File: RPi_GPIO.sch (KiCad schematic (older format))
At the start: 19 parts, among them J1 CONN_02X19, J2 RPi_GPIO, J3 CONN_02X06, J4 CONN_02X06, J5 CONN_02X06, J6 CONN_02X10, J7 CONN_02X10, J8 CONN_02X10, U1 DS1307Z+, U2 CAT24C32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

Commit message: cleanup and add RX/TX header
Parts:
- removed C1: CAP, Capacitors_SMD:C_0805_HandSoldering, symbol CAP
- removed R1: R, Resistors_SMD:R_0805_HandSoldering, symbol R
- added J9: CONN_01X04, Pin_Headers:Pin_Header_Straight_1x04_Pitch2.54mm, symbol CONN_01X04
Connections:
- net 3.3V: now also J3.1 (P1), J8.1 (P1), J9.1 (P1)
- net GND: now also J5.2 (P2), J6.2 (P2), J9.2 (P2)
- net Pin10 renamed RX
- net RX: now also J9.4 (P4)
- net Pin8 renamed TX
- net TX: now also J9.3 (P3)
- no-connect marks 0 -> 1
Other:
- note removed: "100nf"
- note removed: "10K"
- moved on the sheet: J7, J8
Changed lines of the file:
@@
 EESchema Schematic File Version 2
-LIBS:RPi_Hat-rescue
 LIBS:power
 LIBS:device
@@
 LIBS:Zilog
 LIBS:cat24c32
-LIBS:ds1340
 LIBS:RPi_Hat-cache
 EELAYER 25 0
@@
 GND
 Text GLabel 9200 3000 2    60   Input ~ 0
-Pin8
+TX
 Text GLabel 9200 3100 2    60   Input ~ 0
-Pin10
+RX
 Text GLabel 9200 3200 2    60   Input ~ 0
 Pin12
@@
 GND
 Text GLabel 5750 3100 2    60   Input ~ 0
-Pin8
+TX
 Text GLabel 5750 3200 2    60   Input ~ 0
-Pin10
+RX
 Text GLabel 5750 3300 2    60   Input ~ 0
 Pin12
@@
 Text GLabel 4350 7100 3    60   Input ~ 0
 GND
-$Comp
-L R R1
-U 1 1 598AB3BE
-P 5200 6200
-F 0 "R1" V 5280 6200 50  0000 C CNN
-F 1 "R" V 5200 6200 50  0000 C CNN
-F 2 "Resistors_SMD:R_0805_HandSoldering" V 5130 6200 50  0001 C CNN
-F 3 "" H 5200 6200 50  0001 C CNN
-	1    5200 6200
-	0    -1   -1   0
-$EndComp
-$Comp
-L CAP C1
-U 1 1 598AB3EF
-P 5800 6200
-F 0 "C1" V 5900 6350 50  0000 C CNN
-F 1 "CAP" V 5900 6050 50  0000 C CNN
-F 2 "Capacitors_SMD:C_0805_HandSoldering" H 5800 6200 50  0001 C CNN
-F 3 "" H 5800 6200 50  0001 C CNN
-	1    5800 6200
-	0    -1   -1   0
-$EndComp
-Text GLabel 6050 6200 2    60   Input ~ 0
-GND
-Text Notes 5900 6450 2    60   ~ 0
-100nf
-Text Notes 5300 6350 2    60   ~ 0
-10K
 Text Notes 3050 5950 2    60   ~ 0
 32.768Hz
@@
 	4350 7500 4950 7500
 Wire Wire Line
-	4950 6200 5050 6200
-Wire Wire Line
-	5350 6200 5550 6200
-Wire Wire Line
 	3000 2150 2650 2150
 Wire Wire Line
@@
 L CONN_02X10 J7
 U 1 1 598D0311
-P 2600 5150
-F 0 "J7" H 2600 5700 50  0000 C CNN
-F 1 "CONN_02X10" V 2600 5150 50  0000 C CNN
-F 2 "Pin_Headers:Pin_Header_Straight_2x10_Pitch2.54mm" H 2600 3950 50  0001 C CNN
-F 3 "" H 2600 3950 50  0001 C CNN
-	1    2600 5150
+P 2800 5150
+F 0 "J7" H 2800 5700 50  0000 C CNN
+F 1 "CONN_02X10" V 2800 5150 50  0000 C CNN
+F 2 "Pin_Headers:Pin_Header_Straight_2x10_Pitch2.54mm" H 2800 3950 50  0001 C CNN
+F 3 "" H 2800 3950 50  0001 C CNN
+	1    2800 5150
 	1    0    0    -1
 $EndComp
@@
 L CONN_02X10 J8
 U 1 1 598D0360
-P 3200 5150
-F 0 "J8" H 3200 5700 50  0000 C CNN
-F 1 "CONN_02X10" V 3200 5150 50  0000 C CNN
-F 2 "Pin_Headers:Pin_Header_Straight_2x10_Pitch2.54mm" H 3200 3950 50  0001 C CNN
-F 3 "" H 3200 3950 50  0001 C CNN
-	1    3200 5150
-	1    0    0    -1
-$EndComp
+P 3650 5200
+F 0 "J8" H 3650 5750 50  0000 C CNN
+F 1 "CONN_02X10" V 3650 5200 50  0000 C CNN
+F 2 "Pin_Headers:Pin_Header_Straight_2x10_Pitch2.54mm" H 3650 4000 50  0001 C CNN
+F 3 "" H 3650 4000 50  0001 C CNN
+	1    3650 5200
+	1    0    0    -1
+$EndComp
+NoConn ~ 4950 6200
+$Comp
+L CONN_01X04 J9
+U 1 1 59918E85
+P 8700 5800
+F 0 "J9" H 8700 6050 50  0000 C CNN
+F 1 "CONN_01X04" V 8800 5800 50  0000 C CNN
+F 2 "Pin_Headers:Pin_Header_Straight_1x04_Pitch2.54mm" H 8700 5800 50  0001 C CNN
+F 3 "" H 8700 5800 50  0001 C CNN
+	1    8700 5800
+	1    0    0    -1
+$EndComp
+Text GLabel 8500 5650 0    60   Input ~ 0
+3.3V
+Text GLabel 8500 5750 0    60   Input ~ 0
+GND
+Text GLabel 8500 5850 0    60   Input ~ 0
+TX
+Text GLabel 8500 5950 0    60   Input ~ 0
+RX
+Text GLabel 3400 4750 0    60   Input ~ 0
+3.3V
+Text GLabel 2250 4700 2    60   Input ~ 0
+GND
+Text GLabel 1750 3850 0    60   Input ~ 0
+3.3V
+Text GLabel 3450 3850 2    60   Input ~ 0
+GND
 $EndSCHEMATC

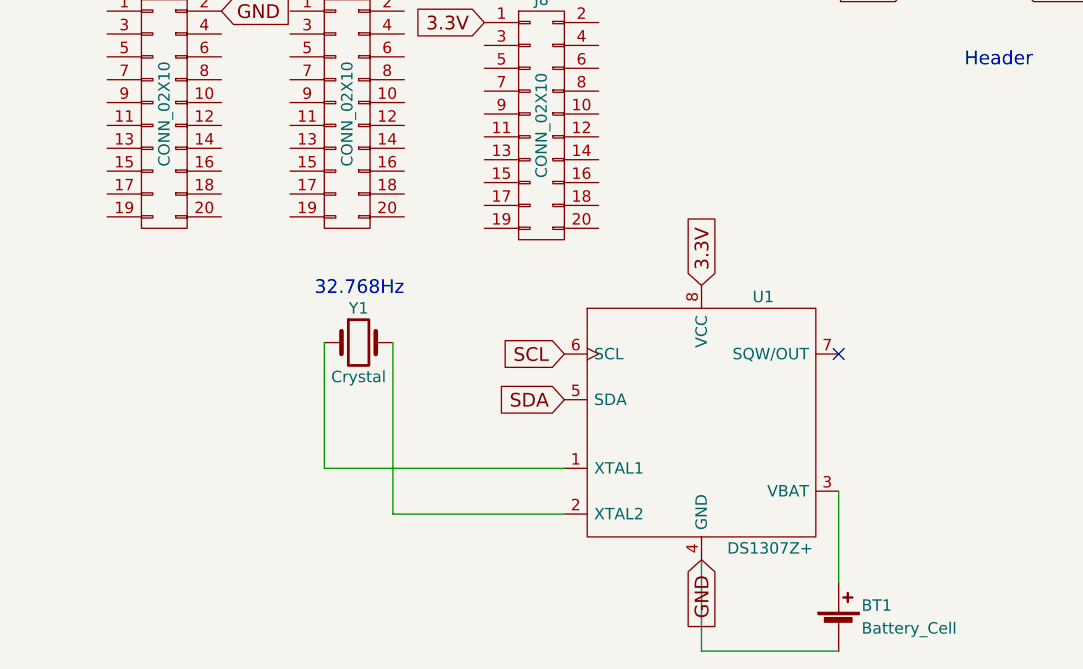
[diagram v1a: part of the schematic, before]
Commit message: support MCP7940N as well as ds1338/ds1340
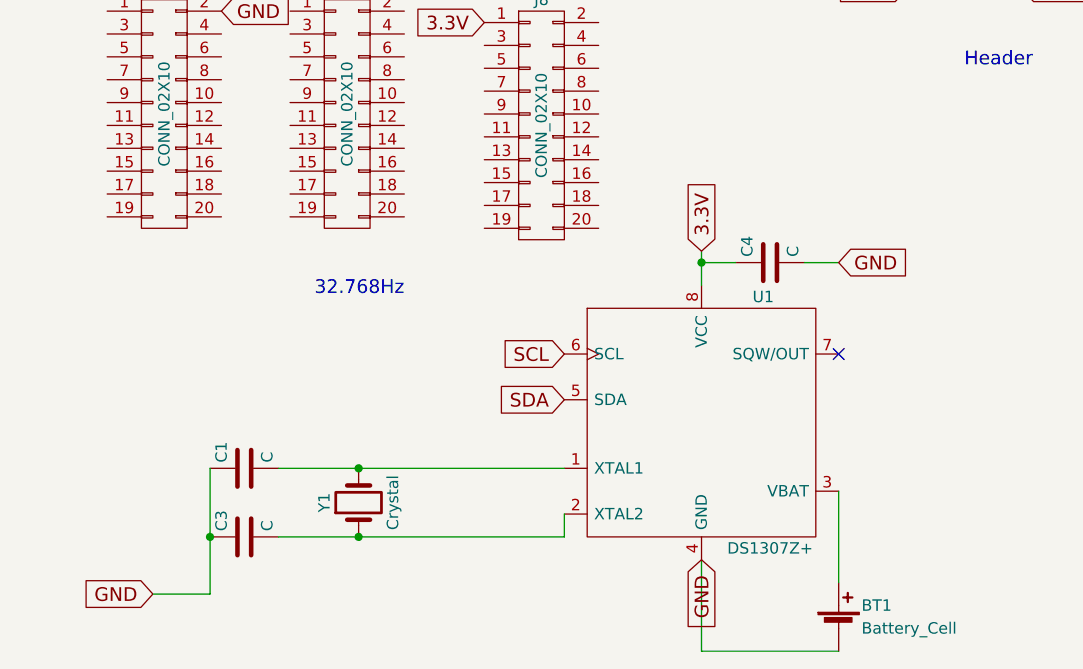
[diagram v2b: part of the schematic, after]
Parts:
- added C1, C3, C4: C, Capacitors_SMD:C_0805_HandSoldering, symbol C
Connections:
- net 3.3V: now also C4.1
- net GND: now also C1.1, C3.1, C4.2
- net at Y1.1: now also U1.2 (XTAL2), C3.2; no longer U1.1 (XTAL1)
- net at Y1.2: now also U1.1 (XTAL1), C1.2; no longer U1.2 (XTAL2)
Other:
- moved on the sheet: Y1
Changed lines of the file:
@@
 L Crystal Y1
 U 1 1 598A4A0E
-P 2850 6150
-F 0 "Y1" H 2850 6300 50  0000 C CNN
-F 1 "Crystal" H 2850 6000 50  0000 C CNN
-F 2 "Crystals:Crystal_SMD_EuroQuartz_EQ161-2pin_3.2x1.5mm_HandSoldering" H 2850 6150 50  0001 C CNN
-F 3 "" H 2850 6150 50  0001 C CNN
-	1    2850 6150
-	1    0    0    -1
+P 2850 6850
+F 0 "Y1" H 2850 7000 50  0000 C CNN
+F 1 "Crystal" H 2850 6700 50  0000 C CNN
+F 2 "Crystals:Crystal_SMD_EuroQuartz_EQ161-2pin_3.2x1.5mm_HandSoldering" H 2850 6850 50  0001 C CNN
+F 3 "" H 2850 6850 50  0001 C CNN
+	1    2850 6850
+	0    -1   -1   0
 $EndComp
 $Comp
@@
 	1    0    0    -1
 $EndComp
-Text GLabel 4350 5900 1    60   Input ~ 0
+Text GLabel 4350 5750 1    60   Input ~ 0
 3.3V
 Text GLabel 3750 6400 0    60   Input ~ 0
@@
 Text Notes 3700 2000 0    60   ~ 0
 3.9K
-Wire Wire Line
-	3750 6700 2700 6700
-Wire Wire Line
-	2700 6700 2700 6150
-Wire Wire Line
-	3750 6900 3000 6900
-Wire Wire Line
-	3000 6900 3000 6150
-Wire Wire Line
-	4950 6800 4950 7200
-Wire Wire Line
-	4350 7100 4350 7500
-Wire Wire Line
-	4350 7500 4950 7500
-Wire Wire Line
-	3000 2150 2650 2150
-Wire Wire Line
-	3000 1350 3000 2150
-Wire Wire Line
-	2700 1600 3000 1600
-Connection ~ 3000 1600
-Wire Wire Line
-	2650 2550 4050 2550
-Wire Wire Line
-	2650 2750 4050 2750
-Wire Wire Line
-	3250 1700 3250 1350
-Wire Wire Line
-	3600 1350 3600 1700
-Wire Wire Line
-	3950 1350 3950 1700
-Wire Wire Line
-	3950 2750 3950 2000
-Connection ~ 3950 2750
-Wire Wire Line
-	3600 2000 3600 2550
-Connection ~ 3600 2550
-Wire Wire Line
-	3250 2350 3250 2000
-Wire Wire Line
-	2650 2350 3250 2350
 $Comp
 L Jumper_NO_Small JP1
@@
 	1    0    0    -1
 $EndComp
-Wire Wire Line
-	3100 3050 3100 2350
-Connection ~ 3100 2350
 Text GLabel 3700 3050 2    60   Input ~ 0
 GND
-Wire Wire Line
-	3300 3050 3700 3050
 Text GLabel 2200 1600 0    60   Input ~ 0
 GND
@@
 Text GLabel 3450 3850 2    60   Input ~ 0
 GND
+Text GLabel 4950 5800 2    60   Input ~ 0
+GND
+$Comp
+L C C4
+U 1 1 599368AB
+P 4650 5800
+F 0 "C4" H 4675 5900 50  0000 L CNN
+F 1 "C" H 4675 5700 50  0000 L CNN
+F 2 "Capacitors_SMD:C_0805_HandSoldering" H 4688 5650 50  0001 C CNN
+F 3 "" H 4650 5800 50  0001 C CNN
+	1    4650 5800
+	0    -1   -1   0
+$EndComp
+Wire Wire Line
+	3000 6900 3000 6900
+Wire Wire Line
+	4950 6800 4950 7200
+Wire Wire Line
+	4350 7100 4350 7500
+Wire Wire Line
+	4350 7500 4950 7500
+Wire Wire Line
+	3000 2150 2650 2150
+Wire Wire Line
+	3000 1350 3000 2150
+Wire Wire Line
+	2700 1600 3000 1600
+Connection ~ 3000 1600
+Wire Wire Line
+	2650 2550 4050 2550
+Wire Wire Line
+	2650 2750 4050 2750
+Wire Wire Line
+	3250 1700 3250 1350
+Wire Wire Line
+	3600 1350 3600 1700
+Wire Wire Line
+	3950 1350 3950 1700
+Wire Wire Line
+	3950 2750 3950 2000
+Connection ~ 3950 2750
+Wire Wire Line
+	3600 2000 3600 2550
+Connection ~ 3600 2550
+Wire Wire Line
+	3250 2350 3250 2000
+Wire Wire Line
+	2650 2350 3250 2350
+Wire Wire Line
+	3100 3050 3100 2350
+Connection ~ 3100 2350
+Wire Wire Line
+	3300 3050 3700 3050
+Wire Wire Line
+	4350 5750 4350 5900
+Wire Wire Line
+	4350 5800 4500 5800
+Connection ~ 4350 5800
+Wire Wire Line
+	4800 5800 4950 5800
+Wire Wire Line
+	2500 6700 3750 6700
+Wire Wire Line
+	2500 7000 3750 7000
+Wire Wire Line
+	3750 7000 3750 6900
+$Comp
+L C C1
+U 1 1 5993707D
+P 2350 6700
+F 0 "C1" H 2375 6800 50  0000 L CNN
+F 1 "C" H 2375 6600 50  0000 L CNN
+F 2 "Capacitors_SMD:C_0805_HandSoldering" H 2388 6550 50  0001 C CNN
+F 3 "" H 2350 6700 50  0001 C CNN
+	1    2350 6700
+	0    -1   -1   0
+$EndComp
+$Comp
+L C C3
+U 1 1 599370EB
+P 2350 7000
+F 0 "C3" H 2375 7100 50  0000 L CNN
+F 1 "C" H 2375 6900 50  0000 L CNN
+F 2 "Capacitors_SMD:C_0805_HandSoldering" H 2388 6850 50  0001 C CNN
+F 3 "" H 2350 7000 50  0001 C CNN
+	1    2350 7000
+	0    -1   -1   0
+$EndComp
+Connection ~ 2850 6700
+Connection ~ 2850 7000
+Wire Wire Line
+	2200 6700 2200 7250
+Text GLabel 1950 7250 0    60   Input ~ 0
+GND
+Wire Wire Line
+	2200 7250 1950 7250
+Connection ~ 2200 7000
 $EndSCHEMATC

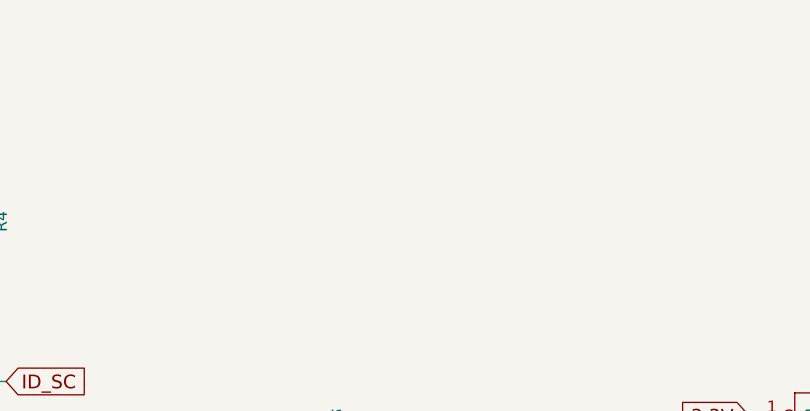
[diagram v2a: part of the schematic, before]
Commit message: add room for an rgb led
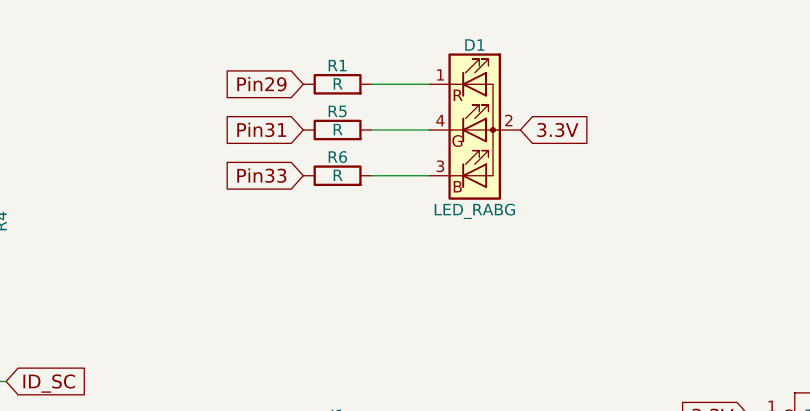
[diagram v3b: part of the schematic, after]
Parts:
- added D1: LED_RABG, symbol LED_RABG
- added R1, R5, R6: R, Resistors_SMD:R_0805_HandSoldering, symbol R
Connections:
- net 3.3V: now also D1.2 (A)
- net Pin29: now also R1.1
- net Pin31: now also R5.1
- net Pin33: now also R6.1
- new net: D1.1 (RK), R1.2
- new net: D1.4 (GK), R5.2
- new net: D1.3 (BK), R6.2
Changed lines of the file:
@@
 	2200 7250 1950 7250
 Connection ~ 2200 7000
+Text GLabel 6300 1450 2    60   Input ~ 0
+3.3V
+Text GLabel 5350 1650 0    60   Input ~ 0
+Pin33
+Text GLabel 5350 1450 0    60   Input ~ 0
+Pin31
+Text GLabel 5350 1250 0    60   Input ~ 0
+Pin29
+$Comp
+L R R1
+U 1 1 59938267
+P 5500 1250
+F 0 "R1" V 5580 1250 50  0000 C CNN
+F 1 "R" V 5500 1250 50  0000 C CNN
+F 2 "Resistors_SMD:R_0805_HandSoldering" V 5430 1250 50  0001 C CNN
+F 3 "" H 5500 1250 50  0001 C CNN
+	1    5500 1250
+	0    -1   -1   0
+$EndComp
+$Comp
+L R R5
+U 1 1 5993838B
+P 5500 1450
+F 0 "R5" V 5580 1450 50  0000 C CNN
+F 1 "R" V 5500 1450 50  0000 C CNN
+F 2 "Resistors_SMD:R_0805_HandSoldering" V 5430 1450 50  0001 C CNN
+F 3 "" H 5500 1450 50  0001 C CNN
+	1    5500 1450
+	0    -1   -1   0
+$EndComp
+$Comp
+L R R6
+U 1 1 599383E3
+P 5500 1650
+F 0 "R6" V 5580 1650 50  0000 C CNN
+F 1 "R" V 5500 1650 50  0000 C CNN
+F 2 "Resistors_SMD:R_0805_HandSoldering" V 5430 1650 50  0001 C CNN
+F 3 "" H 5500 1650 50  0001 C CNN
+	1    5500 1650
+	0    -1   -1   0
+$EndComp
+Wire Wire Line
+	5650 1250 5900 1250
+Wire Wire Line
+	5650 1450 5900 1450
+Wire Wire Line
+	5650 1650 5900 1650
+$Comp
+L LED_RABG D1
+U 1 1 59938EE6
+P 6100 1450
+F 0 "D1" H 6100 1820 50  0000 C CNN
+F 1 "LED_RABG" H 6100 1100 50  0000 C CNN
+F 2 "" H 6100 1400 50  0001 C CNN
+F 3 "" H 6100 1400 50  0001 C CNN
+	1    6100 1450
+	1    0    0    -1
+$EndComp
 $EndSCHEMATC

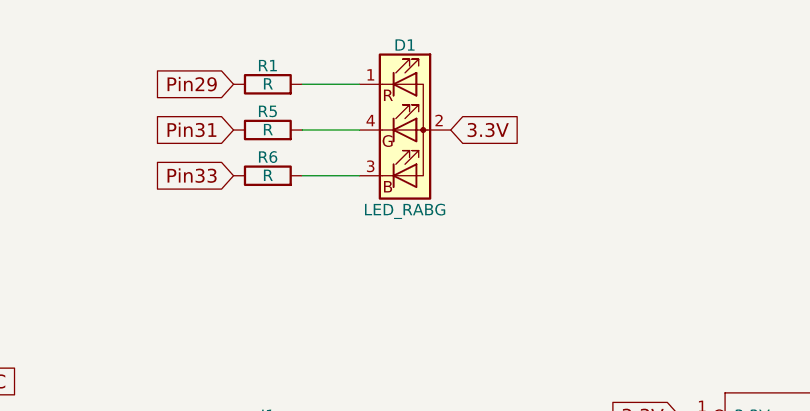
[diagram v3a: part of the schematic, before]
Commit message: use connector footprint for LED as the standard one violated the DRC
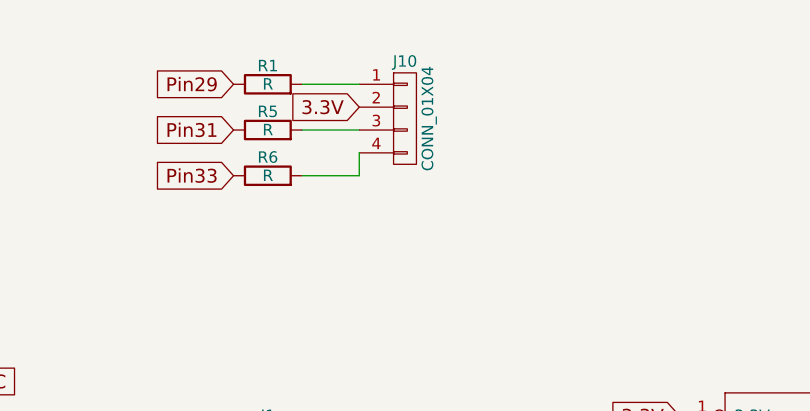
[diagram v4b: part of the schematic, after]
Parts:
- removed D1: LED_RABG, symbol LED_RABG
- added J10: CONN_01X04, Pin_Headers:Pin_Header_Straight_1x04_Pitch1.27mm, symbol CONN_01X04
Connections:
- net 3.3V: now also J10.2 (P2)
- net at R1.2: now also J10.1 (P1)
- net at R5.2: now also J10.3 (P3)
- net at R6.2: now also J10.4 (P4)
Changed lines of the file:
@@
 	2200 7250 1950 7250
 Connection ~ 2200 7000
-Text GLabel 6300 1450 2    60   Input ~ 0
+Text GLabel 5900 1350 0    60   Input ~ 0
 3.3V
 Text GLabel 5350 1650 0    60   Input ~ 0
@@
 	5650 1450 5900 1450
 Wire Wire Line
-	5650 1650 5900 1650
+	5900 1650 5650 1650
 $Comp
-L LED_RABG D1
-U 1 1 59938EE6
-P 6100 1450
-F 0 "D1" H 6100 1820 50  0000 C CNN
-F 1 "LED_RABG" H 6100 1100 50  0000 C CNN
-F 2 "" H 6100 1400 50  0001 C CNN
+L CONN_01X04 J10
+U 1 1 59938516
+P 6100 1400
+F 0 "J10" H 6100 1650 50  0000 C CNN
+F 1 "CONN_01X04" V 6200 1400 50  0000 C CNN
+F 2 "Pin_Headers:Pin_Header_Straight_1x04_Pitch1.27mm" H 6100 1400 50  0001 C CNN
 F 3 "" H 6100 1400 50  0001 C CNN
-	1    6100 1450
+	1    6100 1400
 	1    0    0    -1
 $EndComp
+Wire Wire Line
+	5900 1550 5900 1650
 $EndSCHEMATC

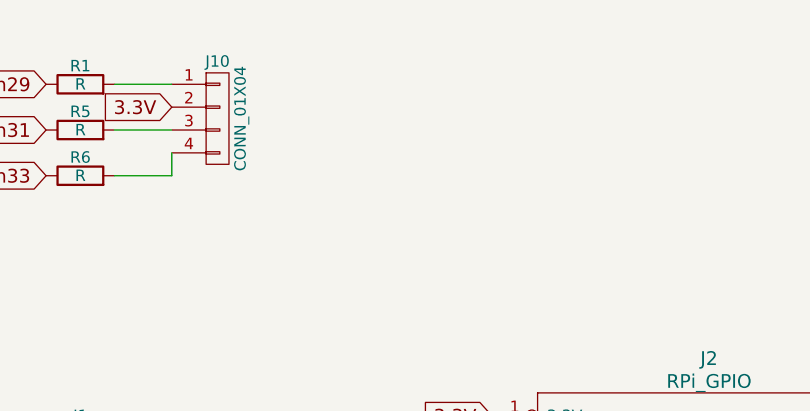
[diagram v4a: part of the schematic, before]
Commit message: support SMD RGB LED as well
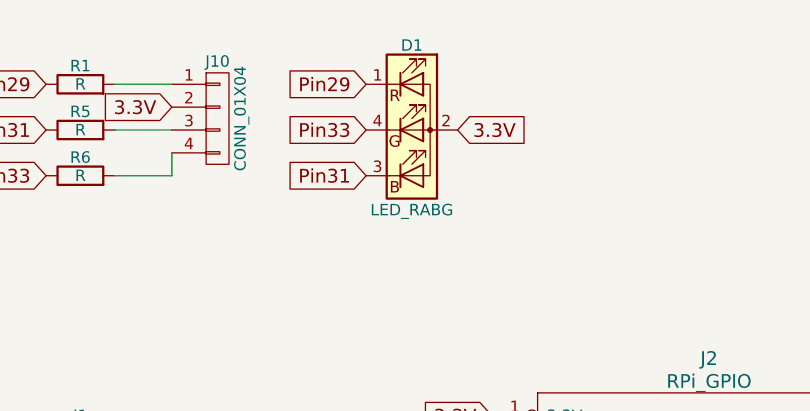
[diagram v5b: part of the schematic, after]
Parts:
- added D1: LED_RABG, LEDs:LED_WS2812B-PLCC4, symbol LED_RABG
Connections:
- net 3.3V: now also D1.2 (A)
- net Pin29: now also D1.1 (RK)
- net Pin31: now also D1.3 (BK)
- net Pin33: now also D1.4 (GK)
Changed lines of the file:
@@
 Wire Wire Line
 	5900 1550 5900 1650
+$Comp
+L LED_RABG D1
+U 1 1 59939910
+P 6950 1450
+F 0 "D1" H 6950 1820 50  0000 C CNN
+F 1 "LED_RABG" H 6950 1100 50  0000 C CNN
+F 2 "LEDs:LED_WS2812B-PLCC4" H 6950 1400 50  0001 C CNN
+F 3 "" H 6950 1400 50  0001 C CNN
+	1    6950 1450
+	1    0    0    -1
+$EndComp
+Text GLabel 7150 1450 2    60   Input ~ 0
+3.3V
+Text GLabel 6750 1250 0    60   Input ~ 0
+Pin29
+Text GLabel 6750 1650 0    60   Input ~ 0
+Pin31
+Text GLabel 6750 1450 0    60   Input ~ 0
+Pin33
 $EndSCHEMATC

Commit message: remove SMD LED
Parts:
- removed D1: LED_RABG, LEDs:LED_WS2812B-PLCC4, symbol LED_RABG
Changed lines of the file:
@@
 Text GLabel 2200 1600 0    60   Input ~ 0
 GND
-Text GLabel 3250 1350 1    60   Input ~ 0
-3.3V
-Text GLabel 3600 1350 1    60   Input ~ 0
-3.3V
-Text GLabel 3950 1350 1    60   Input ~ 0
-3.3V
 $Comp
 L CONN_02X06 J3
@@
 	3000 1350 3000 2150
 Wire Wire Line
-	2700 1600 3000 1600
+	2700 1600 3950 1600
 Connection ~ 3000 1600
 Wire Wire Line
@@
 Wire Wire Line
 	2650 2750 4050 2750
-Wire Wire Line
-	3250 1700 3250 1350
-Wire Wire Line
-	3600 1350 3600 1700
-Wire Wire Line
-	3950 1350 3950 1700
 Wire Wire Line
 	3950 2750 3950 2000
@@
 Wire Wire Line
 	5900 1550 5900 1650
-$Comp
-L LED_RABG D1
-U 1 1 59939910
-P 6950 1450
-F 0 "D1" H 6950 1820 50  0000 C CNN
-F 1 "LED_RABG" H 6950 1100 50  0000 C CNN
-F 2 "LEDs:LED_WS2812B-PLCC4" H 6950 1400 50  0001 C CNN
-F 3 "" H 6950 1400 50  0001 C CNN
-	1    6950 1450
-	1    0    0    -1
-$EndComp
-Text GLabel 7150 1450 2    60   Input ~ 0
-3.3V
-Text GLabel 6750 1250 0    60   Input ~ 0
-Pin29
-Text GLabel 6750 1650 0    60   Input ~ 0
-Pin31
-Text GLabel 6750 1450 0    60   Input ~ 0
-Pin33
+Wire Wire Line
+	3250 1600 3250 1700
+Wire Wire Line
+	3600 1600 3600 1700
+Connection ~ 3250 1600
+Wire Wire Line
+	3950 1600 3950 1700
+Connection ~ 3600 1600
 $EndSCHEMATC
